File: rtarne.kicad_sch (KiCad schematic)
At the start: 26 parts, among them J2 4PIN, U1 ProMicro

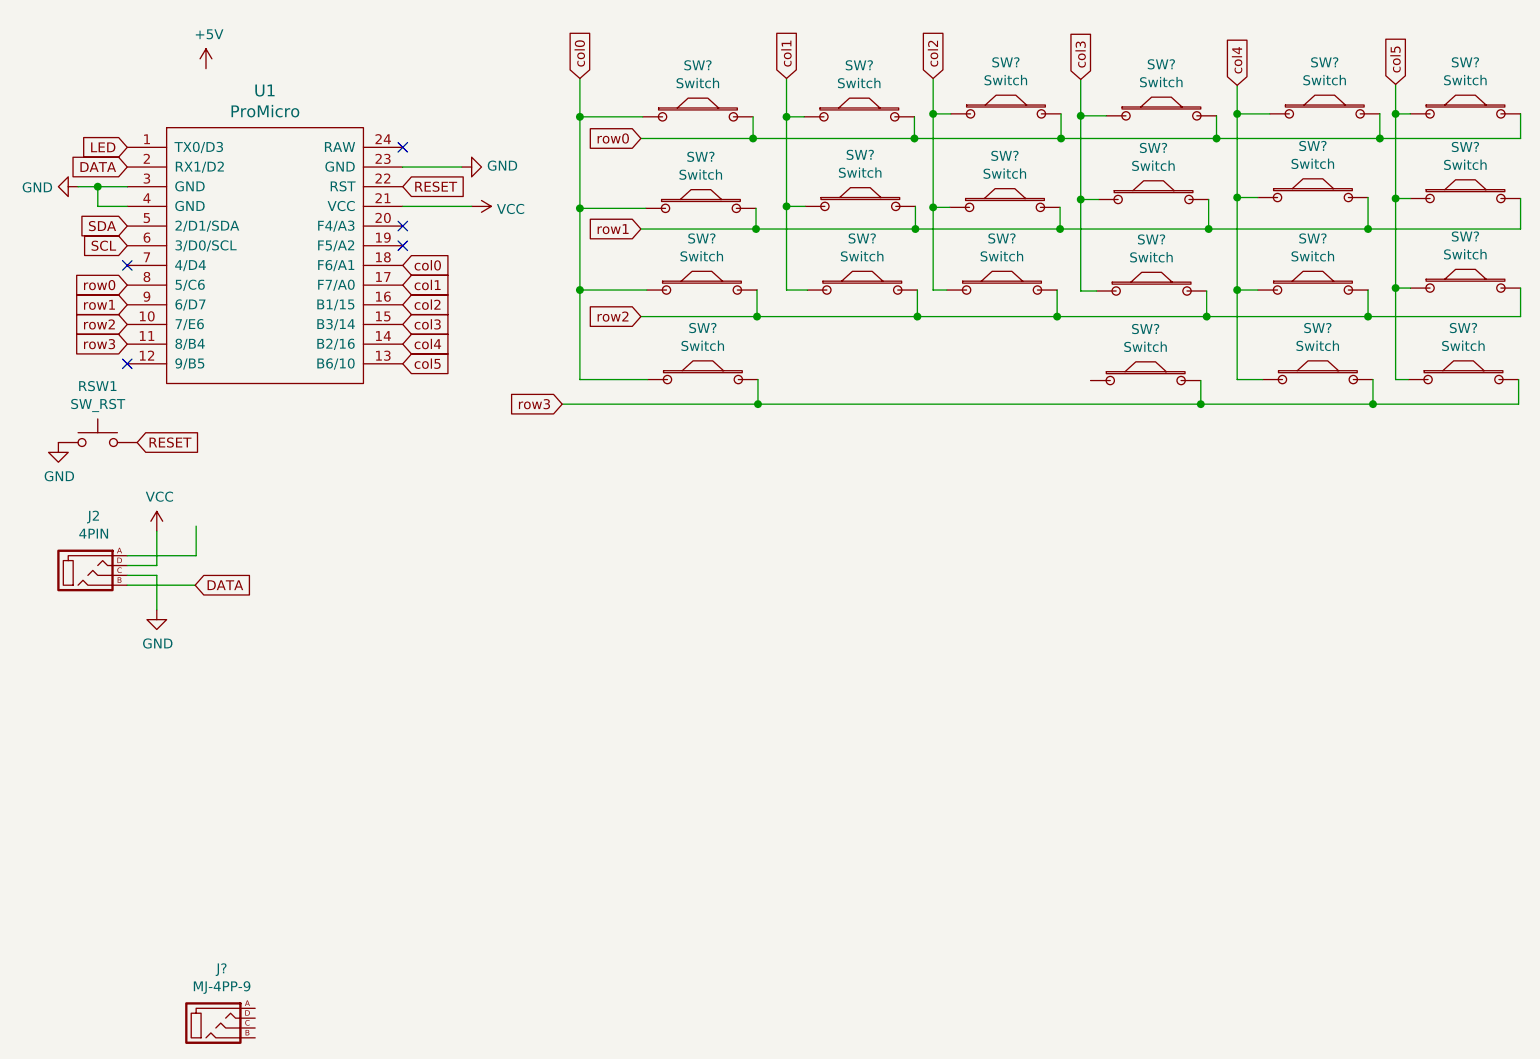
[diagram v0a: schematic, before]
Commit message: Add edge cut and set switch case plase
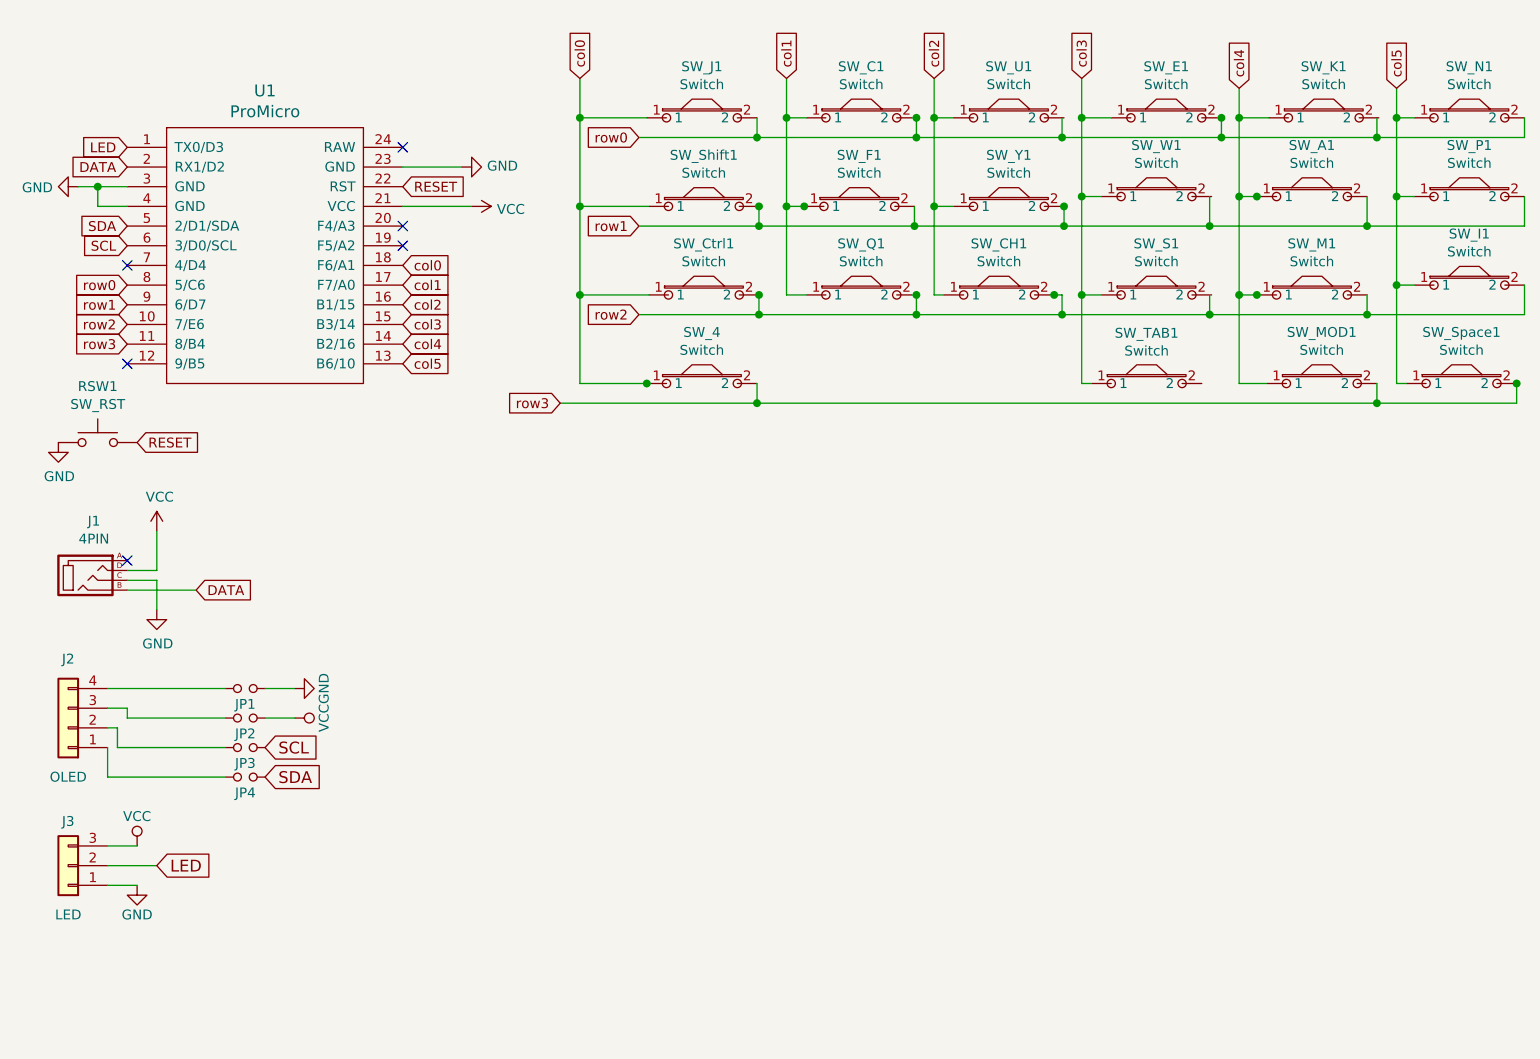
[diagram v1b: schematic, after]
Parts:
- removed J?: MJ-4PP-9, symbol kbd:MJ-4PP-9
- removed SW?: Switch, RTA-80:SW_RTA80, symbol rta80:Switch
- added J2: OLED, kbd:OLED, symbol corne-classic-rescue:Conn_01x04-Connector_Generic
- added J3: LED, kbd:StripLED_rev, symbol corne-classic-rescue:Conn_01x03-Connector_Generic
- added JP1, JP2, JP3, JP4: (no value), kbd:Jumper, symbol corne-classic-rescue:Jumper_NO_Small-Device
- added SW_TAB1: Switch, RTA-80:SW_RTA80, symbol rta80:Switch
- J1: renamed from J2; footprint (none) -> kbd:MJ-4PP-9_1side
- RSW1: footprint (none) -> kbd:ResetSW_1side
- SW_C1, SW_J1: renamed from SW?; footprint (none) -> RTA-80:SW_RTA80
- U1: footprint (none) -> kbd:ProMicro_v3
- gave numbers to parts that had none: 19
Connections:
- net GND: now also J3.1 (Pin_1), JP1.1
- net LED: now also J3.2 (Pin_2)
- net SCL: now also JP3.1
- net SDA: now also JP4.1
- net VCC: now also J3.3 (Pin_3), JP2.1
- net col0: now also SW_4.1, SW_Ctrl1.1, SW_J1.1, SW_Shift1.1; no longer SW_4.~, SW_Ctrl1.~, SW_J1.~, SW_Shift1.~
- net col1: now also SW_C1.1, SW_F1.1, SW_Q1.1; no longer SW_C1.~, SW_F1.~, SW_Q1.~
- net col2: now also SW_CH1.1, SW_U1.1, SW_Y1.1; no longer SW_CH1.~, SW_U1.~, SW_Y1.~
- net col3: now also SW_E1.1, SW_S1.1, SW_W1.1, SW_TAB1.1; no longer SW_E1.~, SW_S1.~, SW_W1.~
- net col4: now also SW_A1.1, SW_K1.1, SW_M1.1, SW_MOD1.1; no longer SW_A1.~, SW_K1.~, SW_M1.~, SW_MOD1.~
- net col5: now also SW_I1.1, SW_N1.1, SW_P1.1, SW_Space1.1; no longer SW_I1.~, SW_N1.~, SW_P1.~, SW_Space1.~
- net row0: now also SW_C1.2, SW_E1.2, SW_J1.2, SW_N1.2; no longer SW_C1.~, SW_E1.~, SW_J1.~, SW_K1.~, SW_N1.~, SW_U1.~
- net row1: now also SW_A1.2, SW_F1.2, SW_P1.2, SW_Shift1.2, SW_Y1.2; no longer SW_A1.~, SW_F1.~, SW_P1.~, SW_Shift1.~, SW_W1.~, SW_Y1.~
- net row2: now also SW_CH1.2, SW_Ctrl1.2, SW_I1.2, SW_M1.2, SW_Q1.2; no longer SW_CH1.~, SW_Ctrl1.~, SW_I1.~, SW_M1.~, SW_Q1.~, SW_S1.~
- net row3: now also SW_4.2, SW_MOD1.2, SW_Space1.2; no longer SW_4.~, SW_MOD1.~, SW_Space1.~
- new net: J2.1 (Pin_1), JP4.2
- new net: J2.2 (Pin_2), JP3.2
- new net: J2.3 (Pin_3), JP2.2
- new net: J2.4 (Pin_4), JP1.2
- no-connect marks 5 -> 6
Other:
- moved on the sheet: J1
